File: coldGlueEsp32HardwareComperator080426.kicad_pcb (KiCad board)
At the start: 2 copper layers, 104 x 93 mm, 75 parts, among them CN1 KF243-5.0-2P, CN2 KF243-5.0-2P, CN3 KF243-5.0-2P, CN4 KF243-5.0-2P, CN5 KF243-5.0-2P, CN6 KF243-5.0-2P, CN7 KF243-5.0-2P, CN9 KF243-5.0-4P, Q1 SQM120P10-10m1L, U1 DRV8262DDWR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

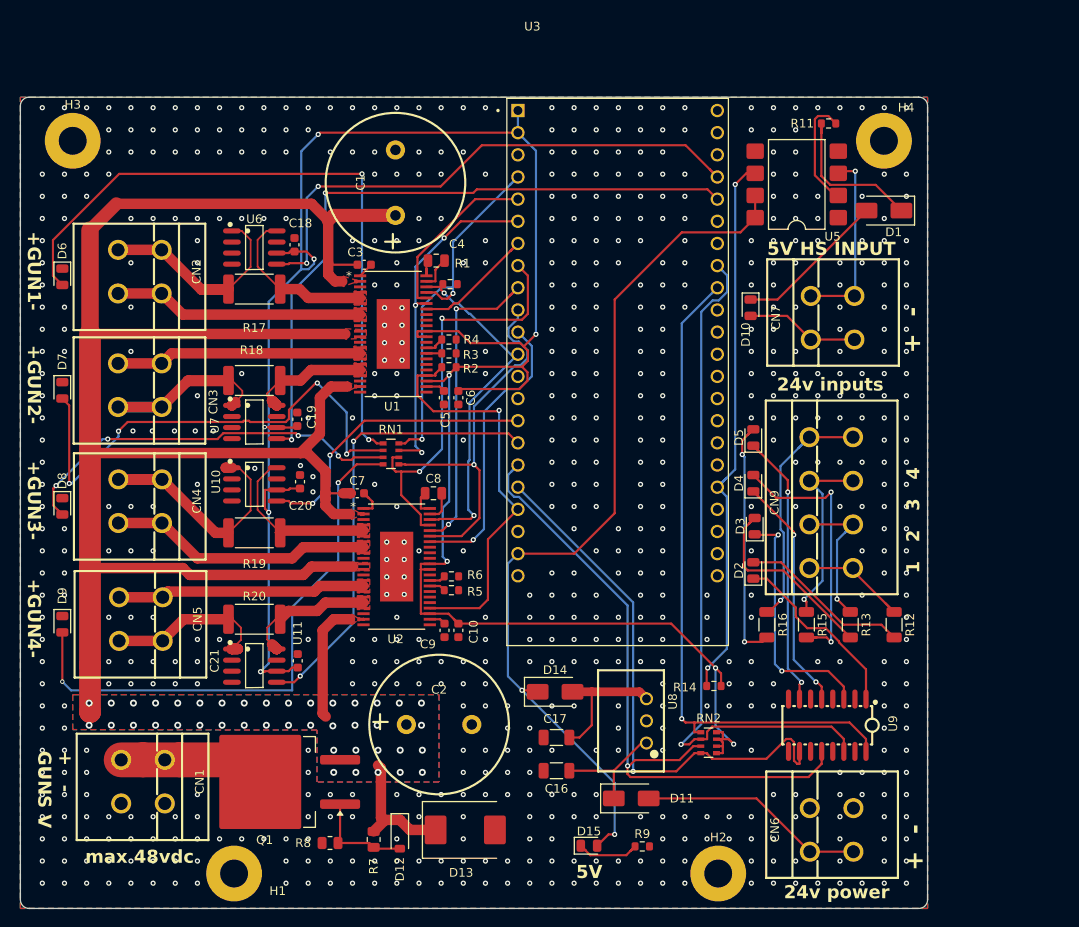
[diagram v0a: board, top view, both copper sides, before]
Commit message: wiring headers and remove esp from board before routing
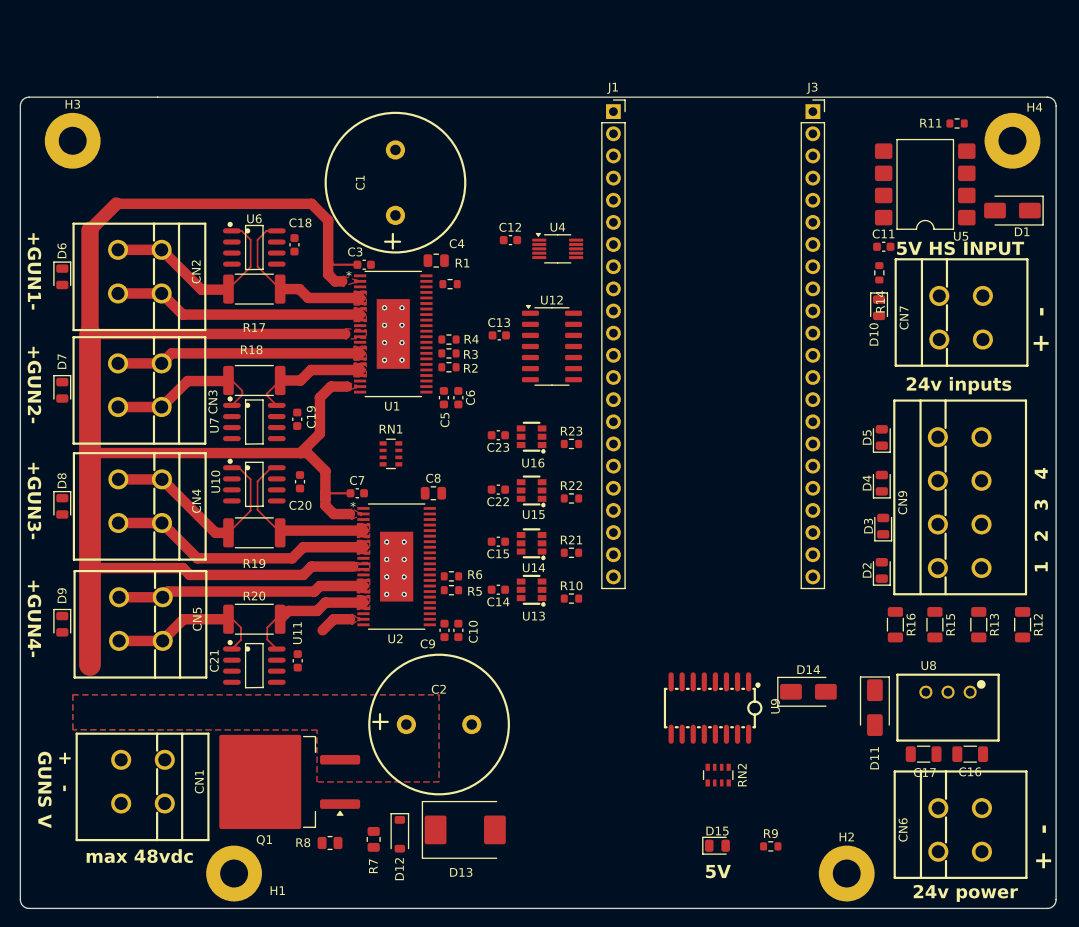
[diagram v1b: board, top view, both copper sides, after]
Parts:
- removed U3: ESP32-S3-DEVKITC-1-N8R8, ESP32-S3-DEVKITC-1-N8R2:XCVR_ESP32-S3-DEVKITC-1-N8R2
- added C11: 100nf 50v, Capacitor_SMD:C_0603_1608Metric, F.Cu at (205.0, 57.1)
- added C12: 100nf 50v, Capacitor_SMD:C_0603_1608Metric, F.Cu at (162.2, 56.4)
- added C13: 100nf 50v, Capacitor_SMD:C_0603_1608Metric, F.Cu at (160.9, 67.3)
- added C14: 100nf 50v, Capacitor_SMD:C_0603_1608Metric, F.Cu at (160.8, 96.5)
- added C15: 100nf 50v, Capacitor_SMD:C_0603_1608Metric, F.Cu at (160.8, 91.0)
- added C22: 100nf 50v, Capacitor_SMD:C_0603_1608Metric, F.Cu at (160.8, 85.0)
- added C23: 100nf 50v, Capacitor_SMD:C_0603_1608Metric, F.Cu at (160.8, 78.8)
- added J1: Female Header 1x22, Connector_PinSocket_2.54mm:PinSocket_1x22_P2.54mm_Vertical, F.Cu at (174.0, 41.7)
- added J3: Female Header 1x22, Connector_PinSocket_2.54mm:PinSocket_1x22_P2.54mm_Vertical, F.Cu at (196.8, 41.7)
- added R10: 10k, Resistor_SMD:R_0603_1608Metric, F.Cu at (169.2, 97.5)
- added R21: 10k, Resistor_SMD:R_0603_1608Metric, F.Cu at (169.2, 92.2)
- added R22: 10k, Resistor_SMD:R_0603_1608Metric, F.Cu at (169.2, 86.0)
- added R23: 10k, Resistor_SMD:R_0603_1608Metric, F.Cu at (169.2, 79.8)
- added U12: LM339, Package_SO:SOIC-14_3.9x8.7mm_P1.27mm, F.Cu at (166.9, 68.6)
- added U13: 74LVC1G157GV,125, easyeda2kicad:TSOP-6_L3.0-W1.5-P0.95-LS2.8-BR, F.Cu at (164.6, 96.5)
- added U14: 74LVC1G157GV,125, easyeda2kicad:TSOP-6_L3.0-W1.5-P0.95-LS2.8-BR, F.Cu at (164.6, 91.1)
- added U15: 74LVC1G157GV,125, easyeda2kicad:TSOP-6_L3.0-W1.5-P0.95-LS2.8-BR, F.Cu at (164.6, 85.1)
- added U16: 74LVC1G157GV,125, easyeda2kicad:TSOP-6_L3.0-W1.5-P0.95-LS2.8-BR, F.Cu at (164.6, 78.9)
- added U4: MCP4728, Package_SO:MSOP-10_3x3mm_P0.5mm, F.Cu at (167.6, 57.4)
- R11: value 330r -> 100r
- R12, R13, R15, R16: value 2.2k -> 4.7k
- R7: value 100k -> 33k
- R8: value 47k -> 100k
- moved R14 51.0 mm to (204.5, 60.1), turned to -90 degrees
- moved C16 47.5 mm to (214.9, 115.3)
- moved C17 42.1 mm to (209.6, 115.3), turned to 0 degrees
- moved U8 34.7 mm to (212.3, 108.2), turned to 180 degrees
- moved D11 29.8 mm to (204.0, 110.0), turned to -90 degrees
- moved D14 29.0 mm to (196.3, 108.2)
- moved CN9 14.7 mm to (213.7, 86.5)
- moved CN6 14.7 mm to (213.7, 124.0)
- moved CN7 14.7 mm to (213.8, 65.3)
- moved D1 14.7 mm to (219.7, 53.0)
- moved D10 14.7 mm to (204.4, 64.1)
- moved D15 14.7 mm to (185.9, 125.8)
- moved D2 14.7 mm to (204.8, 94.3)
- moved D3 14.7 mm to (204.9, 89.2)
- moved D4 14.7 mm to (204.8, 84.3)
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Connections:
- net /Input_0_5v renamed /ENCODER
- net /U1_IN1 renamed /J1_6
- net /U1_IN3 renamed /J1_7
- net /U2_IN1 renamed /J1_8
- net /U2_IN3 renamed /J1_9
- net /nFAULT renamed /J3_9
- C17 pad 1: Net-(D14-A) -> /pure5V
- CN3 pad 1: /U1_OUT4 -> Net-(U7-IN-)
- CN3 pad 2: Net-(U7-IN-) -> /U1_OUT4
- CN5 pad 1: /U2_OUT4 -> Net-(U11-IN-)
- CN5 pad 2: Net-(U11-IN-) -> /U2_OUT4
- D14 pad 2: Net-(D14-A) -> /pure5V
- R1 pad 2: GND -> +3V3
- U10 pad 5: /Gun3Vref -> /Gun3_Sense
- U11 pad 5: /Gun4Vref -> /Gun4_Sense
- U5 pad 7: +5V -> /pure5V
- U5 pad 8: +5V -> /pure5V
- U6 pad 5: /Gun1Vref -> /Gun1_Sense
- U7 pad 5: /Gun2Vref -> /Gun2_Sense
- U8 pad 3: Net-(D14-A) -> /pure5V
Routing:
- net +3V3: track 266.4 -> 0.00 mm, vias 10 -> 0
- net +5V: track 102.2 -> 0.00 mm, vias 2 -> 0
- net /Input_2_24v: track 80.2 -> 0.00 mm, vias 1 -> 0
- net /Input_1_24v: track 78.2 -> 0.00 mm, vias 1 -> 0
- net /Gun2Vref: track 77.2 -> 0.00 mm, vias 2 -> 0
- net Net-(D6-A): track 76.8 -> 0.00 mm, vias 2 -> 0
- net /Input_3_24v: track 76.0 -> 0.00 mm, vias 1 -> 0
- net /ENCODER: track 65.9 -> 0.00 mm, vias 2 -> 0
- net Net-(D9-A): track 64.4 -> 0.00 mm, vias 2 -> 0
- net /Input_4_24v: track 64.0 -> 0.00 mm, vias 1 -> 0
- net /Gun1Vref: track 63.2 -> 0.00 mm, vias 2 -> 0
- net Net-(D7-A): track 58.3 -> 0.00 mm, vias 4 -> 0
- net /Gun4Vref: track 52.1 -> 0.00 mm, vias 2 -> 0
- net /J1_8: track 48.2 -> 0.00 mm, vias 2 -> 0
- net /J3_9: track 46.8 -> 0.00 mm, vias 1 -> 0
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- removed copper zone on B.Cu, net GND
- removed copper zone on F.Cu, net GND
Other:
- board size 104 x 93 mm -> 118.7 x 93 mm

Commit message: CN3,5 fix orientation(before  freerouting)
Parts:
- moved C12 7.76 mm to (169.9, 56.9), turned to 90 degrees
- moved C13 7.18 mm to (164.3, 73.6), turned to 90 degrees
- moved U4 2.76 mm to (164.8, 57.1), turned to -90 degrees
- moved U12 1.68 mm to (165.6, 67.6), turned to 90 degrees
- moved J1 0.51 mm to (173.5, 41.7)
- moved J3 0.51 mm to (196.3, 41.7)
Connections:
- CN3 pad 1: Net-(U7-IN-) -> /U1_OUT4
- CN3 pad 2: /U1_OUT4 -> Net-(U7-IN-)
- CN5 pad 1: Net-(U11-IN-) -> /U2_OUT4
- CN5 pad 2: /U2_OUT4 -> Net-(U11-IN-)
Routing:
- net +48V: track 202.8 -> 227.5 mm
- net Net-(Q1-D): track 0.00 -> 17.0 mm
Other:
- board text added: "-GUN2+"
- board text added: "-GUN4+"
- board text removed: "+GUN2-"
- board text removed: "+GUN4-"

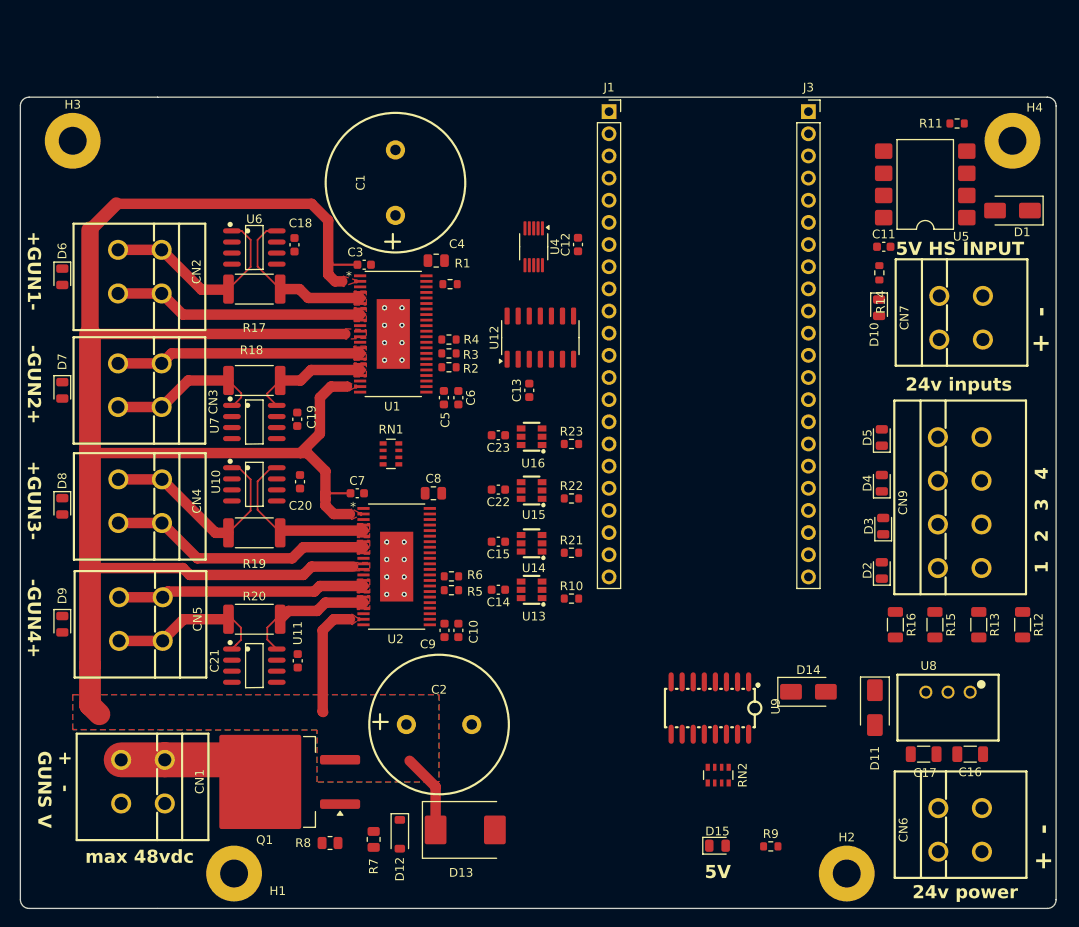
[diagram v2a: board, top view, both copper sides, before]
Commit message: complete routing
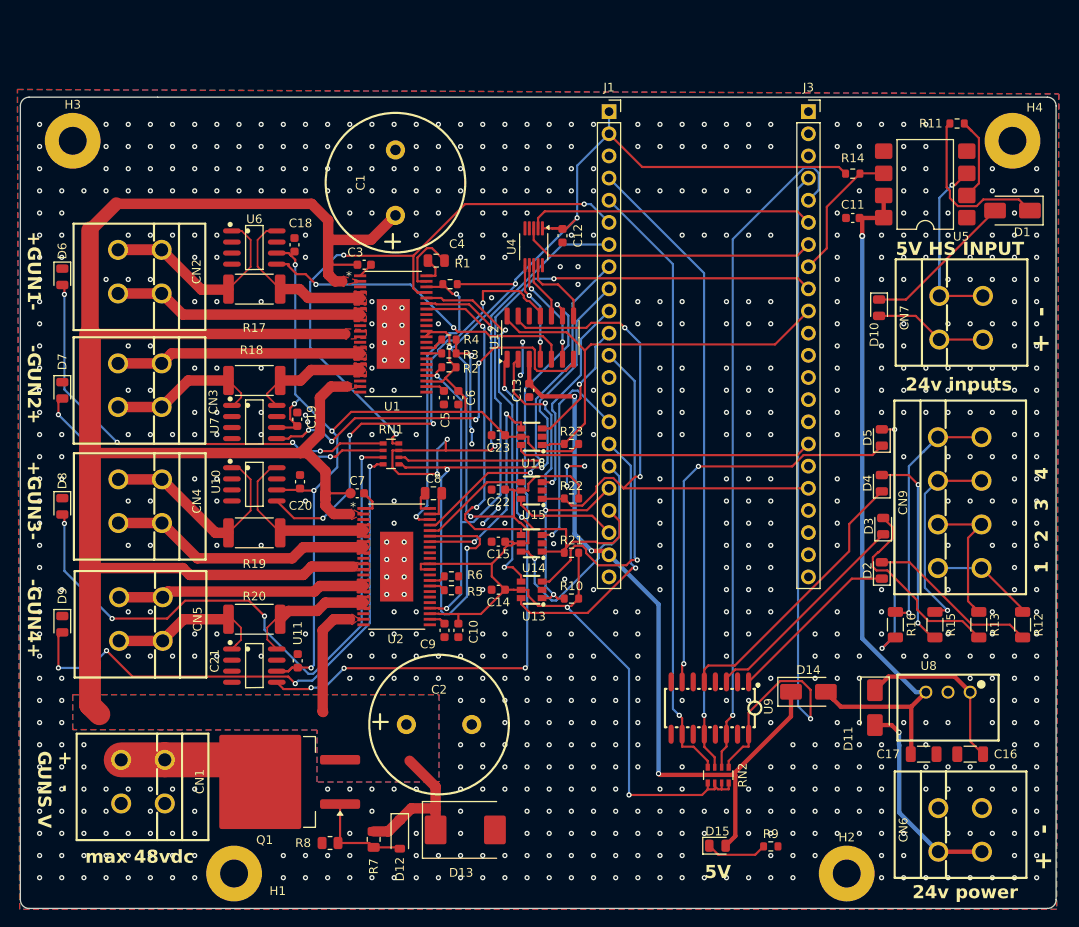
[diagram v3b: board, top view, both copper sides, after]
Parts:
- moved R14 11.8 mm to (201.4, 48.8), turned to 0 degrees
- moved C11 4.85 mm to (201.4, 53.8), turned to 180 degrees
- moved C12 2.05 mm to (168.1, 55.9)
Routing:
- net +3V3: track 0.00 -> 323.9 mm, vias 0 -> 11
- net /J3_9: track 0.00 -> 97.6 mm, vias 0 -> 3
- net +5V: track 0.00 -> 86.4 mm, vias 0 -> 3
- net /Input_1_24v: track 0.00 -> 83.0 mm, vias 0 -> 1
- net /pure5V: track 0.00 -> 82.9 mm, vias 0 -> 1
- net /Input_2_24v: track 0.00 -> 78.2 mm, vias 0 -> 1
- net /Gun4_Sense: track 0.00 -> 76.0 mm, vias 0 -> 4
- net /J1_9: track 0.00 -> 75.6 mm, vias 0 -> 3
- net /Input_3_24v: track 0.00 -> 72.6 mm, vias 0 -> 1
- net Net-(D8-A): track 0.00 -> 72.2 mm, vias 0 -> 4
- net /Input_4_24v: track 0.00 -> 70.5 mm, vias 0 -> 1
- net /J1_6: track 0.00 -> 67.8 mm, vias 0 -> 3
- net /Gun3Interrupt: track 0.00 -> 66.8 mm, vias 0 -> 2
- net /J1_7: track 0.00 -> 66.0 mm, vias 0 -> 4
- net Net-(D9-A): track 0.00 -> 64.8 mm, vias 0 -> 4
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- added copper zone on B.Cu, net GND
- added copper zone on F.Cu, net GND

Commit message: routed no errors
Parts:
- moved R10 26.6 mm to (174.8, 123.5)
- moved R23 26.6 mm to (174.8, 105.8)
- moved U13 26.6 mm to (170.2, 122.5)
- moved U16 26.6 mm to (170.2, 104.9)
- moved R21 26.6 mm to (174.8, 118.2)
- moved R22 26.6 mm to (174.8, 112.0)
- moved U14 26.6 mm to (170.2, 117.2)
- moved U15 26.6 mm to (170.2, 111.1)
- moved C14 26.5 mm to (165.9, 122.5)
- moved C15 26.5 mm to (165.9, 117.0)
- moved C22 26.5 mm to (165.9, 111.0)
- moved C23 26.5 mm to (165.9, 104.8)
- moved U12 8.64 mm to (165.6, 76.2)
- moved C13 8.64 mm to (164.3, 82.2)
- moved H1 0.48 mm to (130.5, 128.5)
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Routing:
- net /U1_IN2: track 42.1 -> 77.5 mm
- net /Gun1Interrupt: track 42.4 -> 74.4 mm, vias 3 -> 4
- net /J1_11: track 14.8 -> 45.8 mm, vias 1 -> 2
- net /J1_10: track 24.0 -> 52.9 mm
- net /U1_IN4: track 38.2 -> 66.0 mm
- net /J1_9: track 75.6 -> 48.5 mm, vias 3 -> 1
- net Net-(D8-A): track 72.2 -> 45.9 mm
- net /Gun4Interrupt: track 52.6 -> 78.4 mm, vias 0 -> 2
- net +3V3: track 323.9 -> 349.6 mm, vias 11 -> 8
- net /J1_15: track 24.3 -> 49.7 mm, vias 1 -> 2
- net GND: track 24.5 -> 1.48 mm, vias 769 -> 18
- net /U2_IN2: track 12.8 -> 35.4 mm, vias 0 -> 2
- net /Gun3Interrupt: track 66.8 -> 89.3 mm, vias 2 -> 1
- net /Gun2Interrupt: track 40.4 -> 61.3 mm, vias 2 -> 3
- net /J1_6: track 67.8 -> 47.0 mm
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
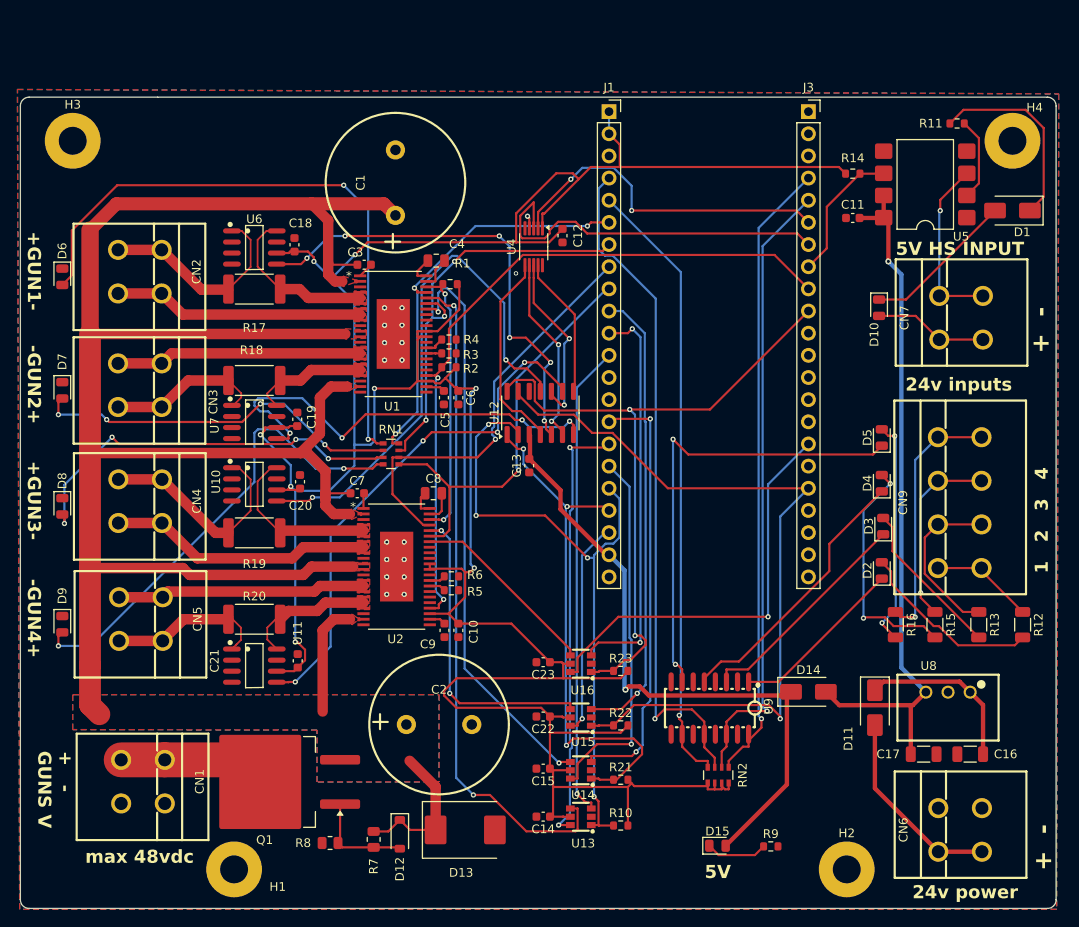
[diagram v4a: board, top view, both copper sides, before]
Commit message: all lcsc part numbers collected
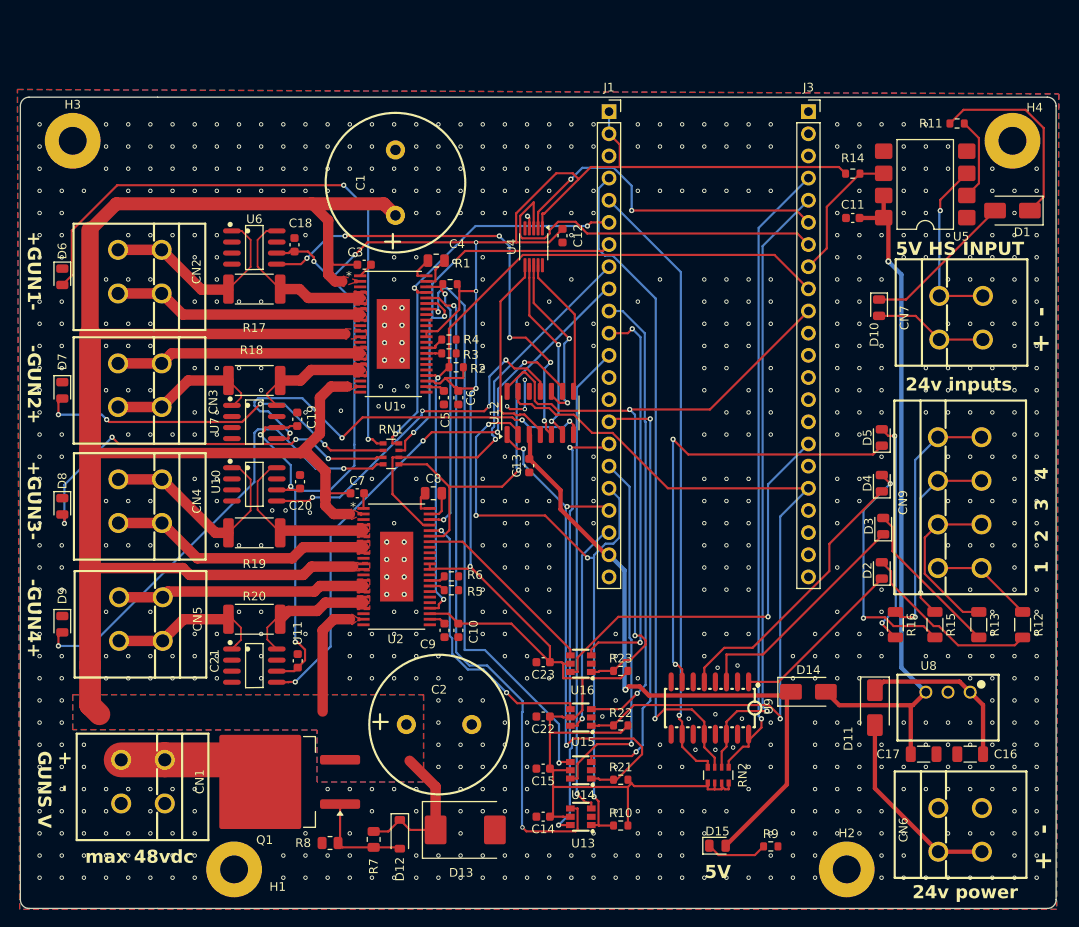
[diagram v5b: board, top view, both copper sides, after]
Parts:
- moved R2 0.83 mm to (156.0, 71.0)
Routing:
- net /Gun3_Sense: track 61.3 -> 41.4 mm, vias 2 -> 4
- net +3V3: track 349.6 -> 333.5 mm, vias 8 -> 9
- net GND: track 1.48 -> 7.01 mm, vias 18 -> 769
- net /U2_IN2: track 35.4 -> 32.5 mm
- net /U1_IN4: track 66.0 -> 67.4 mm
- net Net-(D3-K): track 25.8 -> 26.8 mm
- net Net-(U12A--): track 23.1 -> 24.0 mm
- net /Gun4Interrupt: track 78.4 -> 79.2 mm
- net Net-(D4-K): track 31.5 -> 32.2 mm

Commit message: thickened some 48 traces so i can use 1oz copper thickness safely
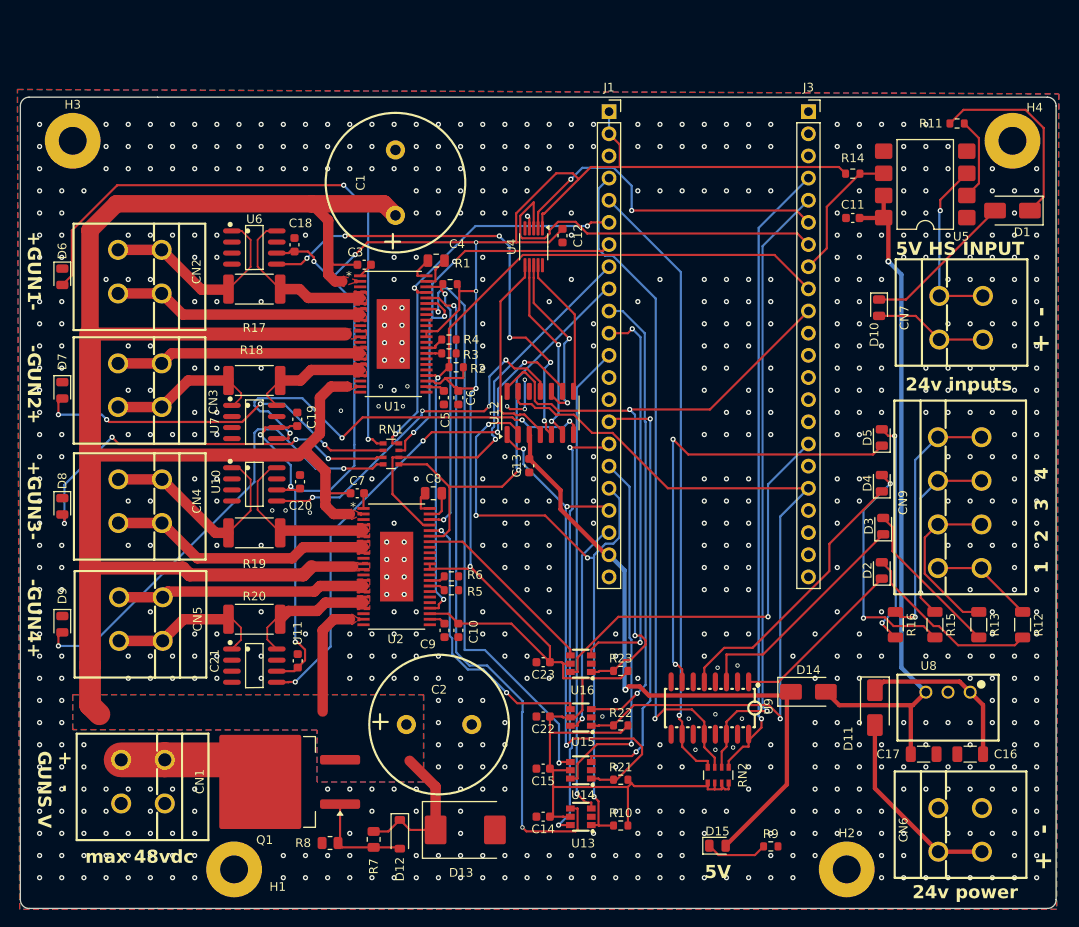
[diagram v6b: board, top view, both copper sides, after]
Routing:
- net GND: vias 769 -> 715
